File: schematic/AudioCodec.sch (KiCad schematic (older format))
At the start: 25 parts, among them U1 TLV320AIC3254IRHBR

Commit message: Rename SM1000neo to ezDV.
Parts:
- U1: footprint SM1000neo:IC_ADS125H01IRHBT -> ezDV:IC_ADS125H01IRHBT
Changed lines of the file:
@@
 F 0 "U1" H 3200 5070 50  0000 C CNN
 F 1 "TLV320AIC3254IRHBR" H 3200 4979 50  0000 C CNN
-F 2 "SM1000neo:IC_ADS125H01IRHBT" H 3200 3400 50  0001 L BNN
+F 2 "ezDV:IC_ADS125H01IRHBT" H 3200 3400 50  0001 L BNN
 F 3 "https://www.ti.com/cn/lit/ds/symlink/tlv320aic3254.pdf?ts=1651153824042" H 3200 3400 50  0001 L BNN
 F 4 "C9925" H 3200 3400 50  0001 C CNN "LCSC"

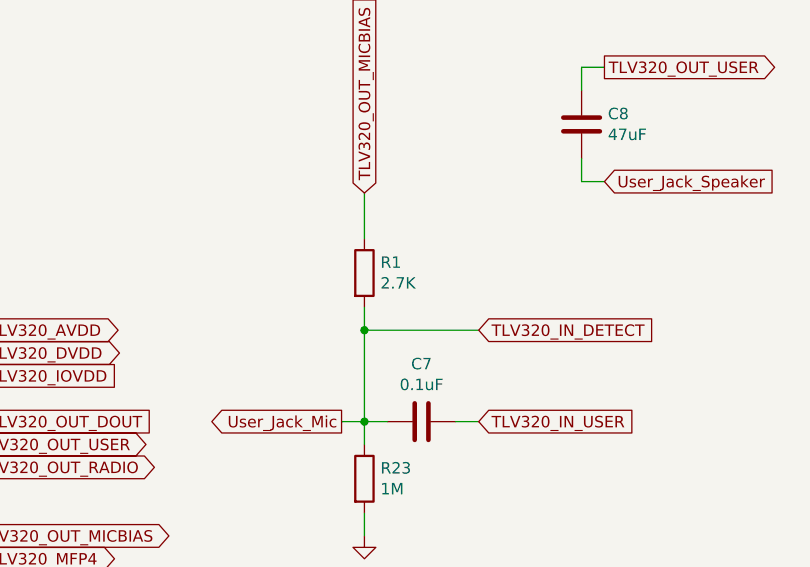
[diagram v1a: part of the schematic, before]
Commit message: Decrease R1 to increase mic bias current (#8).
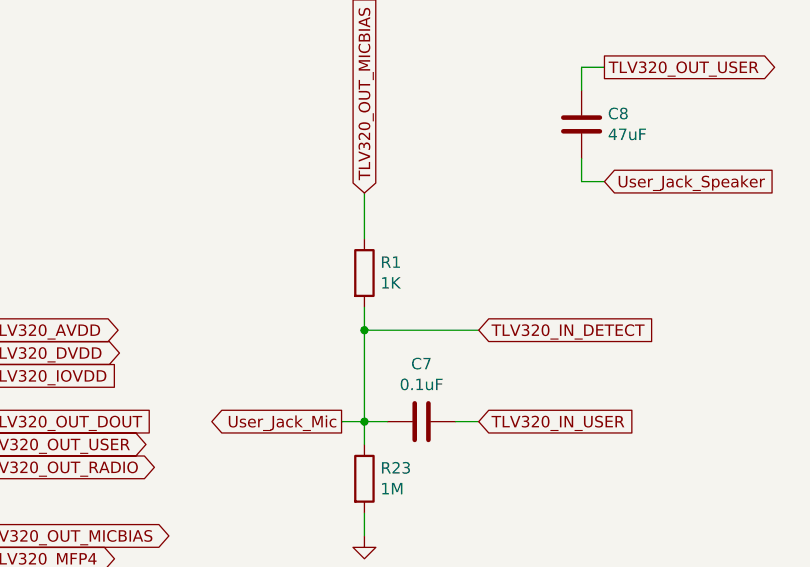
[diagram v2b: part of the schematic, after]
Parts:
- R1: value 2.7K -> 1K; footprint Resistor_SMD:R_0603_1608Metric -> Resistor_SMD:R_0402_1005Metric; LCSC C269437 -> C85373
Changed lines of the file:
@@
 P 6000 1750
 F 0 "R1" H 6070 1796 50  0000 L CNN
-F 1 "2.7K" H 6070 1705 50  0000 L CNN
-F 2 "Resistor_SMD:R_0603_1608Metric" V 5930 1750 50  0001 C CNN
-F 3 "https://datasheet.lcsc.com/lcsc/1811101310_TyoHM-RMC06032-7K5-N_C269437.pdf" H 6000 1750 50  0001 C CNN
-F 4 "C269437" H 6000 1750 50  0001 C CNN "LCSC"
+F 1 "1K" H 6070 1705 50  0000 L CNN
+F 2 "Resistor_SMD:R_0402_1005Metric" V 5930 1750 50  0001 C CNN
+F 3 "https://datasheet.lcsc.com/lcsc/2110260430_UNI-ROYAL-Uniroyal-Elec-0402WGF1021TCE_C85373.pdf" H 6000 1750 50  0001 C CNN
+F 4 "C85373" H 6000 1750 50  0001 C CNN "LCSC"
 	1    6000 1750
 	1    0    0    -1

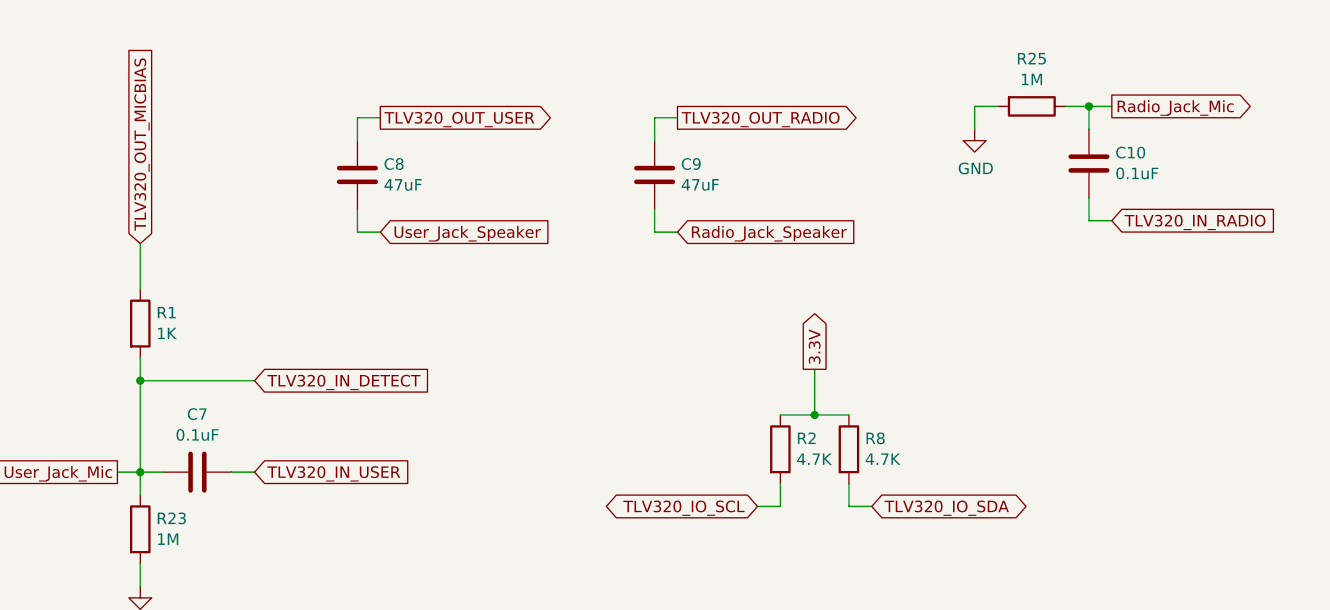
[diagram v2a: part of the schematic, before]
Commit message: Increase C7 and C10 to 0.47uF to match TLV320 EVM (partial solution for #10).
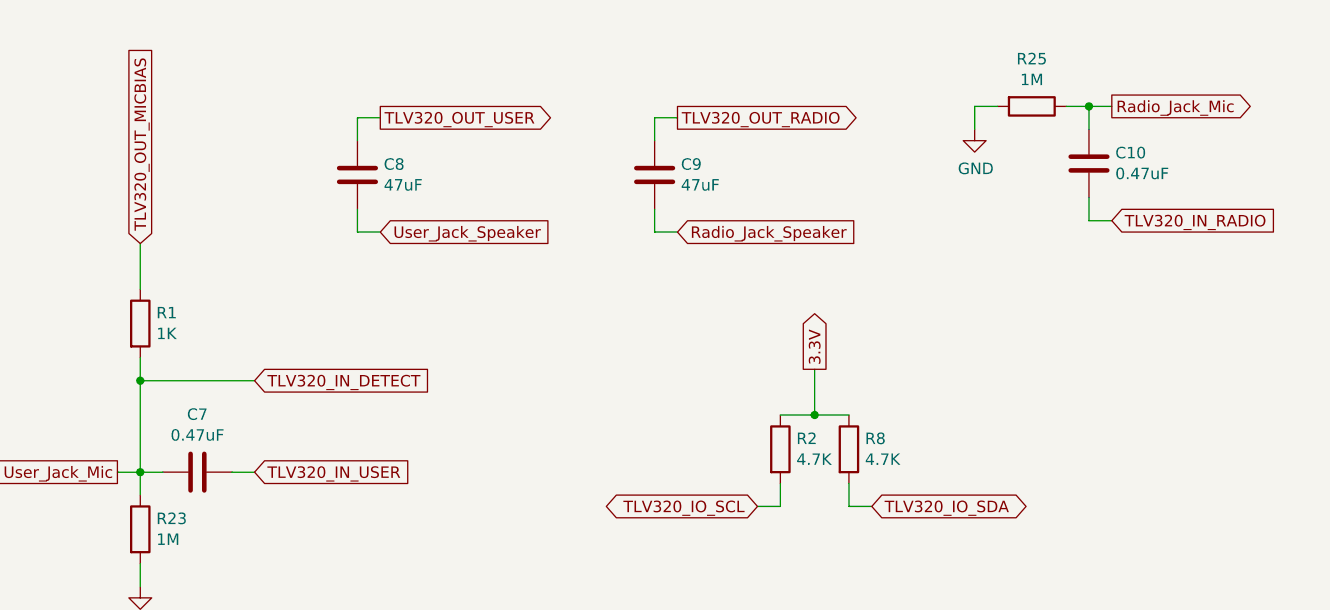
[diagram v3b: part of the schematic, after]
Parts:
- C10, C7: value 0.1uF -> 0.47uF; LCSC C1525 -> C387962
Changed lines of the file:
@@
 P 6250 2400
 F 0 "C7" V 6502 2400 50  0000 C CNN
-F 1 "0.1uF" V 6411 2400 50  0000 C CNN
+F 1 "0.47uF" V 6411 2400 50  0000 C CNN
 F 2 "Capacitor_SMD:C_0402_1005Metric" H 6288 2250 50  0001 C CNN
-F 3 "https://datasheet.lcsc.com/lcsc/1810191219_Samsung-Electro-Mechanics-CL05B104KO5NNNC_C1525.pdf" H 6250 2400 50  0001 C CNN
-F 4 "C1525" H 6250 2400 50  0001 C CNN "LCSC"
+F 3 "https://datasheet.lcsc.com/lcsc/1912111437_Walsin-Tech-Corp-0402X474K250CT_C387962.pdf" H 6250 2400 50  0001 C CNN
+F 4 "C387962" H 6250 2400 50  0001 C CNN "LCSC"
 	1    6250 2400
 	0    -1   -1   0
@@
 P 10150 1050
 F 0 "C10" H 10265 1096 50  0000 L CNN
-F 1 "0.1uF" H 10265 1005 50  0000 L CNN
+F 1 "0.47uF" H 10265 1005 50  0000 L CNN
 F 2 "Capacitor_SMD:C_0402_1005Metric" H 10188 900 50  0001 C CNN
-F 3 "https://datasheet.lcsc.com/lcsc/1810191219_Samsung-Electro-Mechanics-CL05B104KO5NNNC_C1525.pdf" H 10150 1050 50  0001 C CNN
-F 4 "C1525" H 10150 1050 50  0001 C CNN "LCSC"
+F 3 "https://datasheet.lcsc.com/lcsc/1912111437_Walsin-Tech-Corp-0402X474K250CT_C387962.pdf" H 10150 1050 50  0001 C CNN
+F 4 "C387962" H 10150 1050 50  0001 C CNN "LCSC"
 	1    10150 1050
 	1    0    0    -1

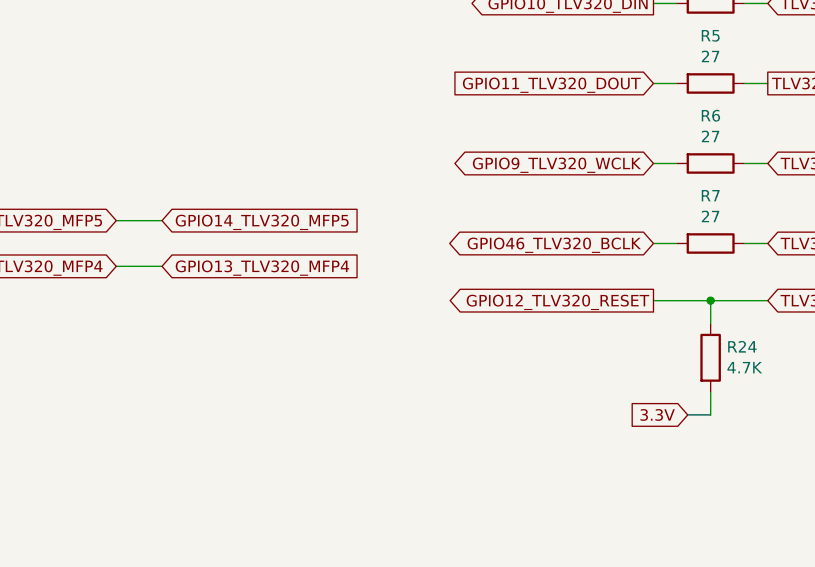
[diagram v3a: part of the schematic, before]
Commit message: Recreated dev platform PCB from scratch;
1. Swapped MFP4 and Reset for TLV320 for ease of routing. (#10)
2. Added vias around outside edge of board. (#1)
3. Added mounting holes for the dev board. (#5)
4. Moved silkscreen labels to improve readability. (#7)
5. Routed sensitive audio traces in inner layer and surrounded by ground vias/planes. (#10)
6. Set mic input capacitor values to same as used on TLV320 EVM to help with noise. (#10)
7. Replaced some parts with 0402 equivalents to help with positioning closer to TLV320. (#10)
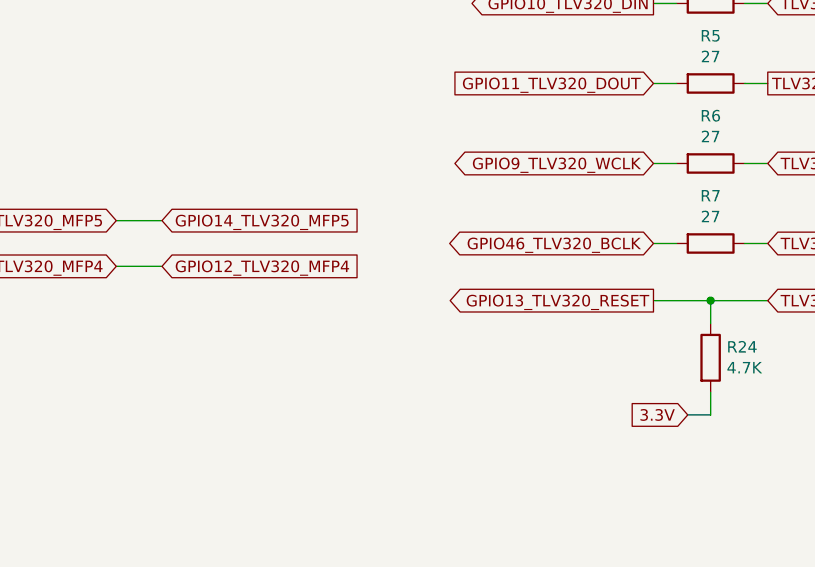
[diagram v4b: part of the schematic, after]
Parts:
- R22: footprint Resistor_SMD:R_0603_1608Metric -> Resistor_SMD:R_0402_1005Metric; LCSC C99782 -> C25900
- R3: footprint Resistor_SMD:R_0603_1608Metric -> Resistor_SMD:R_0402_1005Metric; LCSC C25202 -> C25077
- R4, R5, R6, R7: footprint Resistor_SMD:R_0603_1608Metric -> Resistor_SMD:R_0402_1005Metric; LCSC C25190 -> C31439
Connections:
- net GPIO12_TLV320_RESET renamed GPIO13_TLV320_RESET
- net GPIO13_TLV320_MFP4 renamed GPIO12_TLV320_MFP4
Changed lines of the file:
@@
 F 0 "R3" V 8743 3250 50  0000 C CNN
 F 1 "10" V 8834 3250 50  0000 C CNN
-F 2 "Resistor_SMD:R_0603_1608Metric" V 8880 3250 50  0001 C CNN
-F 3 "https://datasheet.lcsc.com/lcsc/2110252230_UNI-ROYAL-Uniroyal-Elec-0603WAJ0100T5E_C25202.pdf" H 8950 3250 50  0001 C CNN
-F 4 "C25202" H 8950 3250 50  0001 C CNN "LCSC"
+F 2 "Resistor_SMD:R_0402_1005Metric" V 8880 3250 50  0001 C CNN
+F 3 "https://datasheet.lcsc.com/lcsc/2110252230_UNI-ROYAL-Uniroyal-Elec-0402WGF100JTCE_C25077.pdf" H 8950 3250 50  0001 C CNN
+F 4 "C25077" H 8950 3250 50  0001 C CNN "LCSC"
 	1    8950 3250
 	0    1    1    0
@@
 F 0 "R4" V 8743 3600 50  0000 C CNN
 F 1 "27" V 8834 3600 50  0000 C CNN
-F 2 "Resistor_SMD:R_0603_1608Metric" V 8880 3600 50  0001 C CNN
-F 3 "https://datasheet.lcsc.com/lcsc/2110252230_UNI-ROYAL-Uniroyal-Elec-0603WAF270JT5E_C25190.pdf" H 8950 3600 50  0001 C CNN
-F 4 "C25190" H 8950 3600 50  0001 C CNN "LCSC"
+F 2 "Resistor_SMD:R_0402_1005Metric" V 8880 3600 50  0001 C CNN
+F 3 "https://datasheet.lcsc.com/lcsc/2110260230_UNI-ROYAL-Uniroyal-Elec-0402WGF274JTCE_C31439.pdf" H 8950 3600 50  0001 C CNN
+F 4 "C31439" H 8950 3600 50  0001 C CNN "LCSC"
 	1    8950 3600
 	0    1    1    0
@@
 F 0 "R5" V 8743 3950 50  0000 C CNN
 F 1 "27" V 8834 3950 50  0000 C CNN
-F 2 "Resistor_SMD:R_0603_1608Metric" V 8880 3950 50  0001 C CNN
-F 3 "https://datasheet.lcsc.com/lcsc/2110252230_UNI-ROYAL-Uniroyal-Elec-0603WAF270JT5E_C25190.pdf" H 8950 3950 50  0001 C CNN
-F 4 "C25190" H 8950 3950 50  0001 C CNN "LCSC"
+F 2 "Resistor_SMD:R_0402_1005Metric" V 8880 3950 50  0001 C CNN
+F 3 "https://datasheet.lcsc.com/lcsc/2110260230_UNI-ROYAL-Uniroyal-Elec-0402WGF274JTCE_C31439.pdf" H 8950 3950 50  0001 C CNN
+F 4 "C31439" H 8950 3950 50  0001 C CNN "LCSC"
 	1    8950 3950
 	0    1    1    0
@@
 F 0 "R7" V 8743 4650 50  0000 C CNN
 F 1 "27" V 8834 4650 50  0000 C CNN
-F 2 "Resistor_SMD:R_0603_1608Metric" V 8880 4650 50  0001 C CNN
-F 3 "https://datasheet.lcsc.com/lcsc/2110252230_UNI-ROYAL-Uniroyal-Elec-0603WAF270JT5E_C25190.pdf" H 8950 4650 50  0001 C CNN
-F 4 "C25190" H 8950 4650 50  0001 C CNN "LCSC"
+F 2 "Resistor_SMD:R_0402_1005Metric" V 8880 4650 50  0001 C CNN
+F 3 "https://datasheet.lcsc.com/lcsc/2110260230_UNI-ROYAL-Uniroyal-Elec-0402WGF274JTCE_C31439.pdf" H 8950 4650 50  0001 C CNN
+F 4 "C31439" H 8950 4650 50  0001 C CNN "LCSC"
 	1    8950 4650
 	0    1    1    0
@@
 F 0 "R6" V 8743 4300 50  0000 C CNN
 F 1 "27" V 8834 4300 50  0000 C CNN
-F 2 "Resistor_SMD:R_0603_1608Metric" V 8880 4300 50  0001 C CNN
-F 3 "https://datasheet.lcsc.com/lcsc/2110252230_UNI-ROYAL-Uniroyal-Elec-0603WAF270JT5E_C25190.pdf" H 8950 4300 50  0001 C CNN
-F 4 "C25190" H 8950 4300 50  0001 C CNN "LCSC"
+F 2 "Resistor_SMD:R_0402_1005Metric" V 8880 4300 50  0001 C CNN
+F 3 "https://datasheet.lcsc.com/lcsc/2110260230_UNI-ROYAL-Uniroyal-Elec-0402WGF274JTCE_C31439.pdf" H 8950 4300 50  0001 C CNN
+F 4 "C31439" H 8950 4300 50  0001 C CNN "LCSC"
 	1    8950 4300
 	0    1    1    0
@@
 TLV320_RESET
 Text GLabel 8700 4900 0    50   Output ~ 0
-GPIO12_TLV320_RESET
+GPIO13_TLV320_RESET
 Wire Wire Line
 	8700 4900 8950 4900
@@
 GPIO14_TLV320_MFP5
 Text GLabel 6550 4750 2    50   Input ~ 0
-GPIO13_TLV320_MFP4
+GPIO12_TLV320_MFP4
 $Comp
 L power:PWR_FLAG #FLG0103
@@
 F 0 "R22" V 2057 4600 50  0000 C CNN
 F 1 "4.7K" V 1966 4600 50  0000 C CNN
-F 2 "Resistor_SMD:R_0603_1608Metric" V 1780 4600 50  0001 C CNN
-F 3 "https://datasheet.lcsc.com/lcsc/1810231411_YAGEO-RC0603FR-074K7L_C99782.pdf" H 1850 4600 50  0001 C CNN
-F 4 "C99782" H 1850 4600 50  0001 C CNN "LCSC"
+F 2 "Resistor_SMD:R_0402_1005Metric" V 1780 4600 50  0001 C CNN
+F 3 "https://datasheet.lcsc.com/lcsc/2110260030_UNI-ROYAL-Uniroyal-Elec-0402WGF4701TCE_C25900.pdf" H 1850 4600 50  0001 C CNN
+F 4 "C25900" H 1850 4600 50  0001 C CNN "LCSC"
 	1    1850 4600
 	0    -1   -1   0
